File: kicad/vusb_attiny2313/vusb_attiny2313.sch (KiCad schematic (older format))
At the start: 24 parts, among them J1 USB_B_Micro, J2 PORT, J3 PORT B, J4 PORT A, Q1 BSS138, SW1 SW_SPST, U1 LM1117-1.8, U2 ATTINY2313-20PU, U3 MCP23S17, Y1 12Mhz

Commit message: first revision, kernel and avr part work. Kernel code have to be refine
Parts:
- removed SW1: SW_SPST, Buttons_Switches_THT:Nidec_Copal_SH-7010C, symbol Switch:SW_SPST
- added MK1, MK2: Mounting_Hole, Mounting_Holes:MountingHole_3.2mm_M3, symbol Mechanical:Mounting_Hole
- added SW2: SW_DIP_x03, Buttons_Switches_THT:SW_PUSH_x2, symbol Switch:SW_DIP_x03
- J1: footprint Connectors:USB_Mini-B -> Pin_Headers:Pin_Header_Straight_1x04_Pitch2.54mm
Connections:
- net labels added: DATA_CS, DATA_IN, DATA_OUT, DATA_SCK, LED
- wire segments 100 -> 99
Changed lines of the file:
@@
 F 0 "J1" H 1705 2017 50  0000 C CNN
 F 1 "USB_B_Micro" H 1705 1926 50  0000 C CNN
-F 2 "Connectors:USB_Mini-B" H 1800 1500 50  0001 C CNN
+F 2 "Pin_Headers:Pin_Header_Straight_1x04_Pitch2.54mm" H 1800 1500 50  0001 C CNN
 F 3 "~" H 1800 1500 50  0001 C CNN
 	1    1650 1550
@@
 	2850 1650 2600 1650
 Wire Wire Line
-	1950 1350 2200 1350
+	1950 1350 2100 1350
 $Comp
 L device:C_Small C6
@@
 	7500 2450 7500 2550
 $Comp
-L Switch:SW_SPST SW1
-U 1 1 5A423A7A
-P 2400 1350
-F 0 "SW1" H 2400 1585 50  0000 C CNN
-F 1 "SW_SPST" H 2400 1494 50  0000 C CNN
-F 2 "Buttons_Switches_THT:Nidec_Copal_SH-7010C" H 2400 1350 50  0001 C CNN
-F 3 "" H 2400 1350 50  0001 C CNN
-	1    2400 1350
-	1    0    0    -1
-$EndComp
-Wire Wire Line
-	2600 1350 3600 1350
-$Comp
 L Connector:Conn_01x10 J3
 U 1 1 5A423FF6
@@
 Wire Wire Line
 	9800 3500 9450 3500
-Wire Wire Line
-	6550 2700 6750 2700
-Wire Wire Line
-	6750 2250 6750 2700
 $Comp
 L Connector:Conn_01x04 J2
@@
 $EndComp
 Wire Wire Line
-	7500 3700 7500 2800
-Wire Wire Line
 	6750 2250 7200 2250
 Wire Wire Line
-	7500 2800 8450 2800
-Wire Wire Line
-	7600 2900 7600 4000
-Wire Wire Line
-	7600 2900 8450 2900
-Wire Wire Line
-	7700 4100 7700 3000
-Wire Wire Line
 	7700 3000 8450 3000
 Wire Wire Line
-	7800 3100 7800 4200
-Wire Wire Line
-	7800 3100 8450 3100
-Wire Wire Line
 	7050 3100 6550 3100
-Wire Wire Line
-	6550 4000 7600 4000
-Wire Wire Line
-	6550 4100 7700 4100
-Wire Wire Line
-	6550 4200 7800 4200
-Wire Wire Line
-	6550 3700 7500 3700
 Wire Wire Line
 	6550 3000 7050 3000
@@
 Wire Wire Line
 	10450 2800 10500 2800
+$Comp
+L Switch:SW_DIP_x03 SW2
+U 1 1 5A48211F
+P 2400 1350
+F 0 "SW2" H 2400 1817 50  0000 C CNN
+F 1 "SW_DIP_x03" H 2400 1726 50  0000 C CNN
+F 2 "Buttons_Switches_THT:SW_PUSH_x2" H 2400 1350 50  0001 C CNN
+F 3 "" H 2400 1350 50  0001 C CNN
+	1    2400 1350
+	1    0    0    -1
+$EndComp
+Connection ~ 2100 1350
+Connection ~ 2700 1350
+Wire Wire Line
+	2700 1350 3600 1350
+Wire Wire Line
+	2700 1350 2700 1250
+Wire Wire Line
+	2700 1250 2700 1150
+Connection ~ 2700 1250
+Wire Wire Line
+	2100 1150 2100 1250
+Wire Wire Line
+	2100 1250 2100 1350
+Connection ~ 2100 1250
+Text Label 6750 2250 0    50   ~ 0
+LED
+Text Label 7050 4100 2    50   ~ 0
+LED
+Wire Wire Line
+	7050 4100 6550 4100
+Wire Wire Line
+	6550 2700 7050 2700
+Text Label 7050 4200 2    50   ~ 0
+DATA_IN
+Text Label 7700 3000 0    50   ~ 0
+DATA_IN
+Text Label 7050 4000 2    50   ~ 0
+DATA_OUT
+Text Label 7700 3100 0    50   ~ 0
+DATA_OUT
+Wire Wire Line
+	7700 3100 8450 3100
+Wire Wire Line
+	7700 2900 8450 2900
+Wire Wire Line
+	7050 4200 6550 4200
+Text Label 7700 2900 0    50   ~ 0
+DATA_SCK
+Text Label 7050 2700 2    50   ~ 0
+DATA_SCK
+Text Label 7700 2800 0    50   ~ 0
+DATA_CS
+Wire Wire Line
+	7700 2800 8450 2800
+Text Label 7050 3700 2    50   ~ 0
+DATA_CS
+Wire Wire Line
+	6550 3700 7050 3700
+Wire Wire Line
+	6550 4000 7050 4000
+$Comp
+L Mechanical:Mounting_Hole MK2
+U 1 1 5A485C34
+P 1450 6350
+F 0 "MK2" H 1550 6396 50  0000 L CNN
+F 1 "Mounting_Hole" H 1550 6305 50  0000 L CNN
+F 2 "Mounting_Holes:MountingHole_3.2mm_M3" H 1450 6350 50  0001 C CNN
+F 3 "" H 1450 6350 50  0001 C CNN
+	1    1450 6350
+	1    0    0    -1
+$EndComp
+$Comp
+L Mechanical:Mounting_Hole MK1
+U 1 1 5A485DC0
+P 1450 6100
+F 0 "MK1" H 1550 6146 50  0000 L CNN
+F 1 "Mounting_Hole" H 1550 6055 50  0000 L CNN
+F 2 "Mounting_Holes:MountingHole_3.2mm_M3" H 1450 6100 50  0001 C CNN
+F 3 "" H 1450 6100 50  0001 C CNN
+	1    1450 6100
+	1    0    0    -1
+$EndComp
 $EndSCHEMATC

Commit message: add 27c256
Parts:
- removed J3: PORT B, Socket_Strips:Socket_Strip_Straight_1x10_Pitch2.54mm, symbol Connector:Conn_01x10
- removed U3: MCP23S17, Housings_DIP:DIP-28_W7.62mm_LongPads, symbol microchip:MCP23S17
- added U?: 27C256, Package_DIP:DIP-28_W15.24mm, symbol Memory_EPROM:27C256
- C1, C3, C4, C6: symbol device:C_Small -> vusb_attiny2313-rescue:C_Small-device
- C2, C5: symbol device:CP1_Small -> vusb_attiny2313-rescue:CP1_Small-device
- D1: symbol device:LED_Small -> vusb_attiny2313-rescue:LED_Small-device
- ISP1: symbol atmel:AVR-ISP-6 -> vusb_attiny2313-rescue:AVR-ISP-6-atmel
- J2: symbol Connector:Conn_01x04 -> vusb_attiny2313-rescue:Conn_01x04-Connector
- J4: symbol Connector:Conn_01x08 -> vusb_attiny2313-rescue:Conn_01x08-Connector
- MK1, MK2: symbol Mechanical:Mounting_Hole -> vusb_attiny2313-rescue:Mounting_Hole-Mechanical
- Q1: symbol Transistor:BSS138 -> vusb_attiny2313-rescue:BSS138-Transistor
- R1, R2, R3, R4, R5, R6: symbol device:R_Small -> vusb_attiny2313-rescue:R_Small-device
- U1: value LM1117-1.8 -> LM1117-3.3; symbol regul:LM1117-1.8 -> vusb_attiny2313-rescue:LM1117-1.8-regul
- U2: symbol atmel:ATTINY2313-20PU -> vusb_attiny2313-rescue:ATTINY2313-20PU-atmel
- Y1: symbol device:Crystal_Small -> vusb_attiny2313-rescue:Crystal_Small-device
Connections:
- net labels added: D0, D1, D2, D3, D4, D5, D6, D7, D[0..7]
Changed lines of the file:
@@
 $EndDescr
 $Comp
-L atmel:ATTINY2313-20PU U2
+L vusb_attiny2313-rescue:ATTINY2313-20PU-atmel U2
 U 1 1 5A3E5479
 P 5400 3500
@@
 $EndComp
 $Comp
-L regul:LM1117-1.8 U1
+L vusb_attiny2313-rescue:LM1117-1.8-regul U1
 U 1 1 5A3E55A4
 P 4050 1350
 F 0 "U1" H 4050 1592 50  0000 C CNN
-F 1 "LM1117-1.8" H 4050 1501 50  0000 C CNN
+F 1 "LM1117-3.3" H 4050 1501 50  0000 C CNN
 F 2 "TO_SOT_Packages_SMD:SOT-223-3_TabPin2" H 4050 1350 50  0001 C CNN
 F 3 "http://www.ti.com/lit/ds/symlink/lm1117.pdf" H 4050 1350 50  0001 C CNN
@@
 $EndComp
 $Comp
-L device:Crystal_Small Y1
+L vusb_attiny2313-rescue:Crystal_Small-device Y1
 U 1 1 5A3E5771
 P 4000 3100
@@
 $EndComp
 $Comp
-L device:C_Small C3
+L vusb_attiny2313-rescue:C_Small-device C3
 U 1 1 5A3E586E
 P 3650 3500
@@
 $EndComp
 $Comp
-L device:C_Small C4
+L vusb_attiny2313-rescue:C_Small-device C4
 U 1 1 5A3E590E
 P 4000 3500
@@
 $EndComp
 $Comp
-L atmel:AVR-ISP-6 ISP1
+L vusb_attiny2313-rescue:AVR-ISP-6-atmel ISP1
 U 1 1 5A3E59A3
 P 1550 4600
@@
 $EndComp
 $Comp
-L device:R_Small R4
+L vusb_attiny2313-rescue:R_Small-device R4
 U 1 1 5A3E5B40
 P 3100 1150
@@
 $EndComp
 $Comp
-L device:R_Small R3
+L vusb_attiny2313-rescue:R_Small-device R3
 U 1 1 5A3E5BC7
 P 2850 1150
@@
 $EndComp
 $Comp
-L device:R_Small R1
+L vusb_attiny2313-rescue:R_Small-device R1
 U 1 1 5A3E5C29
 P 2200 1550
@@
 $EndComp
 $Comp
-L device:R_Small R2
+L vusb_attiny2313-rescue:R_Small-device R2
 U 1 1 5A3E5CDB
 P 2500 1650
@@
 $EndComp
 $Comp
-L device:CP1_Small C2
+L vusb_attiny2313-rescue:CP1_Small-device C2
 U 1 1 5A3E5D76
 P 3600 1600
@@
 $EndComp
 $Comp
-L device:CP1_Small C5
+L vusb_attiny2313-rescue:CP1_Small-device C5
 U 1 1 5A3E5F04
 P 4600 1600
@@
 $EndComp
 $Comp
-L device:R_Small R5
+L vusb_attiny2313-rescue:R_Small-device R5
 U 1 1 5A3E5F38
 P 3350 2500
@@
 	1950 1350 2100 1350
 $Comp
-L device:C_Small C6
+L vusb_attiny2313-rescue:C_Small-device C6
 U 1 1 5A3E725E
 P 5000 1600
@@
 	3350 2700 4250 2700
 $Comp
-L device:C_Small C1
+L vusb_attiny2313-rescue:C_Small-device C1
 U 1 1 5A3E918A
 P 3350 2900
@@
 Text Label 6850 3900 2    50   ~ 0
 D-
-$Comp
-L microchip:MCP23S17 U3
-U 1 1 5A3F3039
-P 8950 2700
-F 0 "U3" H 8950 2850 50  0000 C CNN
-F 1 "MCP23S17" H 8950 2700 50  0000 C CNN
-F 2 "Housings_DIP:DIP-28_W7.62mm_LongPads" H 9000 1750 50  0001 L CNN
-F 3 "http://ww1.microchip.com/downloads/en/DeviceDoc/20001952C.pdf" H 9200 3700 50  0001 C CNN
-	1    8950 2700
-	-1   0    0    -1
-$EndComp
 Wire Wire Line
 	8450 2400 8000 2400
@@
 $EndComp
 $Comp
-L device:R_Small R6
+L vusb_attiny2313-rescue:R_Small-device R6
 U 1 1 5A400338
 P 7500 1400
@@
 	7500 1200 7500 1300
 $Comp
-L device:LED_Small D1
+L vusb_attiny2313-rescue:LED_Small-device D1
 U 1 1 5A40196B
 P 7500 1700
@@
 $EndComp
 $Comp
-L Transistor:BSS138 Q1
+L vusb_attiny2313-rescue:BSS138-Transistor Q1
 U 1 1 5A406ED6
 P 7400 2250
@@
 	7500 2450 7500 2550
 $Comp
-L Connector:Conn_01x10 J3
-U 1 1 5A423FF6
-P 10700 2300
-F 0 "J3" H 10780 2292 50  0000 L CNN
-F 1 "PORT B" H 10780 2201 50  0000 L CNN
-F 2 "Socket_Strips:Socket_Strip_Straight_1x10_Pitch2.54mm" H 10700 2300 50  0001 C CNN
-F 3 "~" H 10700 2300 50  0001 C CNN
-	1    10700 2300
-	1    0    0    -1
-$EndComp
-$Comp
-L Connector:Conn_01x08 J4
+L vusb_attiny2313-rescue:Conn_01x08-Connector J4
 U 1 1 5A4240DB
 P 10000 3100
@@
 	9800 3500 9450 3500
 $Comp
-L Connector:Conn_01x04 J2
+L vusb_attiny2313-rescue:Conn_01x04-Connector J2
 U 1 1 5A4059D7
 P 7250 2900
@@
 $EndComp
 Wire Wire Line
-	9450 1900 10500 1900
-Wire Wire Line
-	9450 2000 10500 2000
-Wire Wire Line
-	9450 2100 10500 2100
-Wire Wire Line
-	9450 2200 10500 2200
-Wire Wire Line
-	9450 2300 10500 2300
-Wire Wire Line
-	9450 2400 10500 2400
-Wire Wire Line
-	9450 2500 10500 2500
-Wire Wire Line
-	9450 2600 10500 2600
-Wire Wire Line
 	10300 2900 10300 2700
 Wire Wire Line
@@
 	6550 4000 7050 4000
 $Comp
-L Mechanical:Mounting_Hole MK2
+L vusb_attiny2313-rescue:Mounting_Hole-Mechanical MK2
 U 1 1 5A485C34
 P 1450 6350
@@
 $EndComp
 $Comp
-L Mechanical:Mounting_Hole MK1
+L vusb_attiny2313-rescue:Mounting_Hole-Mechanical MK1
 U 1 1 5A485DC0
 P 1450 6100
@@
 	1    0    0    -1
 $EndComp
+$Comp
+L Memory_EPROM:27C256 U?
+U 1 1 5D263362
+P 8950 2600
+F 0 "U?" H 8950 3878 50  0000 C CNN
+F 1 "27C256" H 8950 3787 50  0000 C CNN
+F 2 "Package_DIP:DIP-28_W15.24mm" H 8950 2600 50  0001 C CNN
+F 3 "http://ww1.microchip.com/downloads/en/DeviceDoc/doc0014.pdf" H 8950 2600 50  0001 C CNN
+	1    8950 2600
+	1    0    0    -1
+$EndComp
+Entry Wire Line
+	9550 1700 9650 1800
+Entry Wire Line
+	9550 1800 9650 1900
+Entry Wire Line
+	9550 1900 9650 2000
+Entry Wire Line
+	9550 2000 9650 2100
+Entry Wire Line
+	9550 2100 9650 2200
+Entry Wire Line
+	9550 2200 9650 2300
+Entry Wire Line
+	9550 2300 9650 2400
+Entry Wire Line
+	9550 2400 9650 2500
+Wire Wire Line
+	9350 1700 9550 1700
+Wire Bus Line
+	9650 1500 9650 2650
+Wire Wire Line
+	9350 1800 9550 1800
+Wire Wire Line
+	9350 1900 9550 1900
+Wire Wire Line
+	9350 2000 9550 2000
+Wire Wire Line
+	9350 2100 9550 2100
+Wire Wire Line
+	9350 2200 9550 2200
+Wire Wire Line
+	9350 2300 9550 2300
+Wire Wire Line
+	9350 2400 9550 2400
+Text Label 9400 1700 0    50   ~ 0
+D0
+Text Label 9400 1800 0    50   ~ 0
+D1
+Text Label 9400 1900 0    50   ~ 0
+D2
+Text Label 9400 2000 0    50   ~ 0
+D3
+Text Label 9400 2100 0    50   ~ 0
+D4
+Text Label 9400 2200 0    50   ~ 0
+D5
+Text Label 9400 2300 0    50   ~ 0
+D6
+Text Label 9400 2400 0    50   ~ 0
+D7
+Text Label 9650 1500 3    50   ~ 0
+D[0..7]
 $EndSCHEMATC

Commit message: schematic done
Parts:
- removed C5: 10µ, Capacitors_THT:CP_Radial_D5.0mm_P2.50mm, symbol vusb_attiny2313-rescue:CP1_Small-device
- removed C6: 100n, Capacitors_SMD:C_0805_HandSoldering, symbol vusb_attiny2313-rescue:C_Small-device
- removed J1: USB_B_Micro, Pin_Headers:Pin_Header_Straight_1x04_Pitch2.54mm, symbol Connector:USB_B_Micro
- removed J2: PORT, Socket_Strips:Socket_Strip_Straight_1x04_Pitch2.54mm, symbol vusb_attiny2313-rescue:Conn_01x04-Connector
- removed J4: PORT A, Socket_Strips:Socket_Strip_Straight_1x08_Pitch2.54mm, symbol vusb_attiny2313-rescue:Conn_01x08-Connector
- removed U1: LM1117-3.3, TO_SOT_Packages_SMD:SOT-223-3_TabPin2, symbol vusb_attiny2313-rescue:LM1117-1.8-regul
- added D2, D5: SD 103BW, Diode_SMD:D_SOD-123, symbol Device:D_Schottky_Small
- added D3, D4: 1N4148, Diode_SMD:D_MiniMELF_Handsoldering, symbol Device:D_Small
- added J1: USB, Connector_PinHeader_2.54mm:PinHeader_1x04_P2.54mm_Vertical, symbol Connector_Generic:Conn_01x04
- added Q2: BSS138, Package_TO_SOT_SMD:SOT-23, symbol vusb_attiny2313-rescue:BSS138-Transistor
- added U1, U3, U4: 74HC595, Package_DIP:DIP-16_W7.62mm_Socket_LongPads, symbol 74xx:74HC595
- C1, C3, C4: footprint Capacitors_SMD:C_0805_HandSoldering -> Capacitor_SMD:C_0805_2012Metric_Pad1.15x1.40mm_HandSolder
- C2: footprint Capacitors_THT:CP_Radial_D5.0mm_P2.50mm -> Capacitor_THT:CP_Radial_D5.0mm_P2.50mm
- D1: footprint LEDs:LED_D3.0mm -> LED_THT:LED_D3.0mm
- ISP1: footprint Pin_Headers:Pin_Header_Straight_2x03_Pitch2.54mm -> Connector_PinHeader_2.54mm:PinHeader_2x03_P2.54mm_Vertical
- MK1, MK2: footprint Mounting_Holes:MountingHole_3.2mm_M3 -> MountingHole:MountingHole_3.2mm_M3
- Q1: footprint TO_SOT_Packages_SMD:SOT-23 -> Package_TO_SOT_SMD:SOT-23
- R1, R2, R3, R4, R5: footprint Resistors_SMD:R_1206 -> Resistor_SMD:R_0805_2012Metric_Pad1.15x1.40mm_HandSolder
- R6: value 470 -> 960; footprint Resistors_SMD:R_1206 -> Resistor_SMD:R_0805_2012Metric_Pad1.15x1.40mm_HandSolder
- SW2: footprint Buttons_Switches_THT:SW_PUSH_x2 -> modules:DPDT_WIDE_54_54
- U2: footprint Housings_DIP:DIP-20_W7.62mm -> Package_DIP:DIP-20_W7.62mm_LongPads
- U5: renamed from U?; footprint Package_DIP:DIP-28_W15.24mm -> modules:DIP_Socket-28pin_in_32_W11.9_W12.7_W15.24_W17.78_W18.5_3M_232-1285-00-0602J
- Y1: footprint Crystals:Crystal_SMD_HC49-SD -> Crystal:Crystal_HC49-U_Vertical
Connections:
- net labels added: +12V, +5V, A10, A11, A12, A13, A14, A8, A9, A9_, A9_set, DATA_CLR, DATA_Q, DATA_R, VPP, VPP_set, ~CE, ~OE, ~VPP
- net labels removed: DATA_OUT, INTA, INTB, LED
- wire segments 99 -> 138
- no-connect marks 2 -> 7
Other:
- moved on the sheet: C1, C3, C4, D1, ISP1, MK1, MK2, Q1, R5, R6, U2, U5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

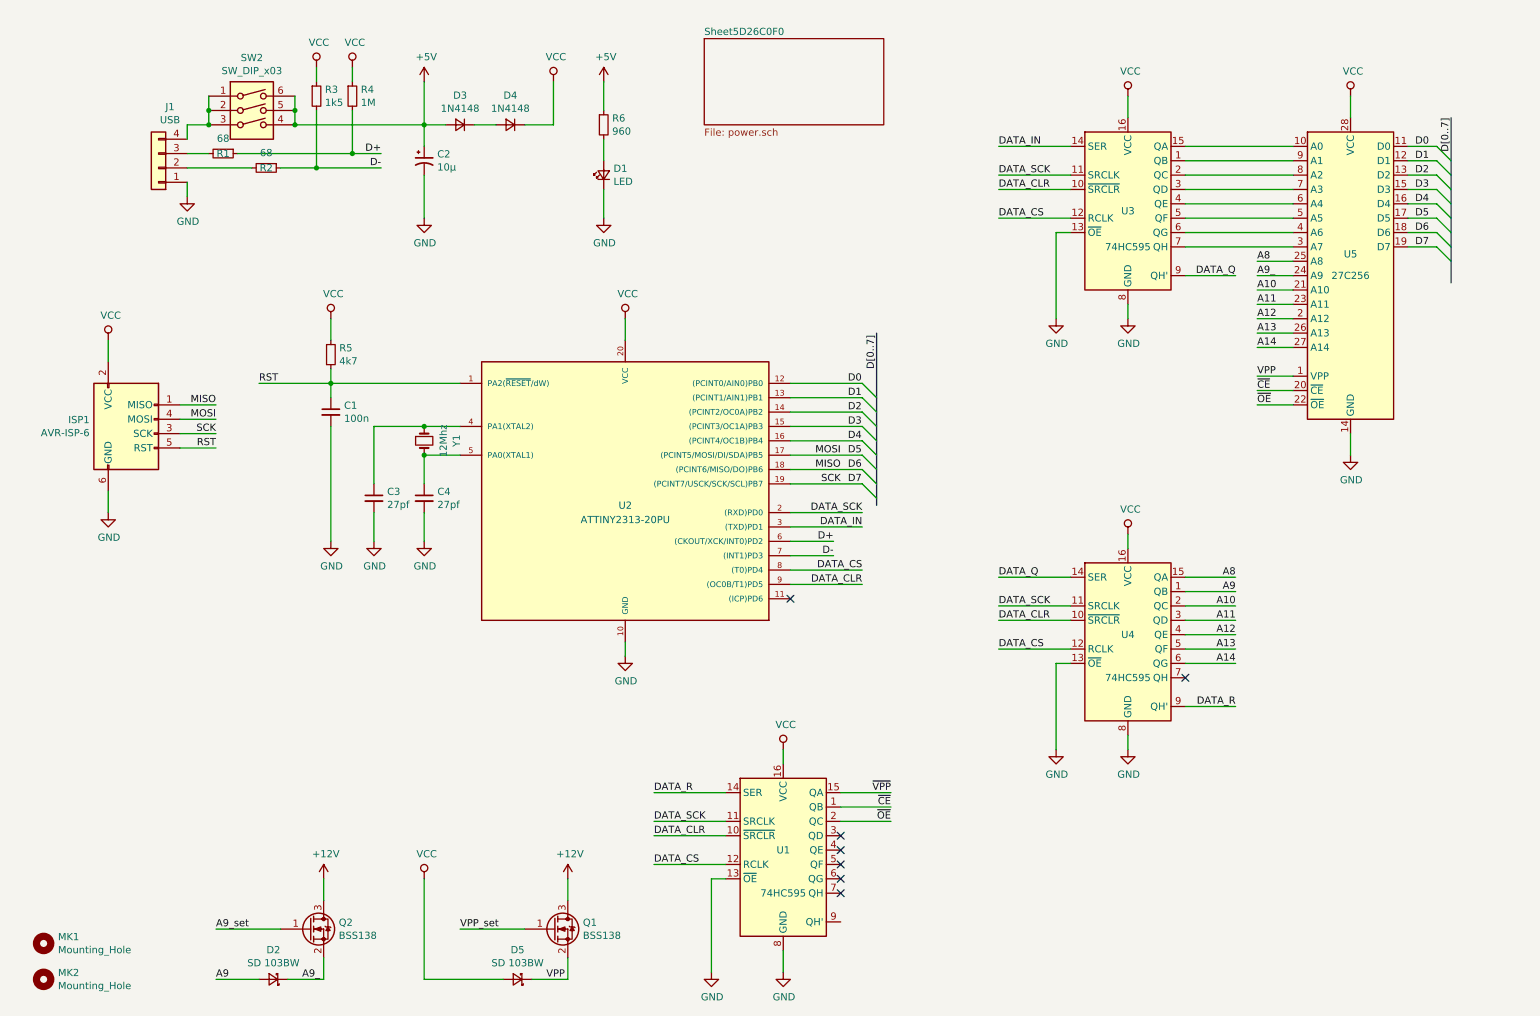
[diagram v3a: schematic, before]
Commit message: fuses angepasst!
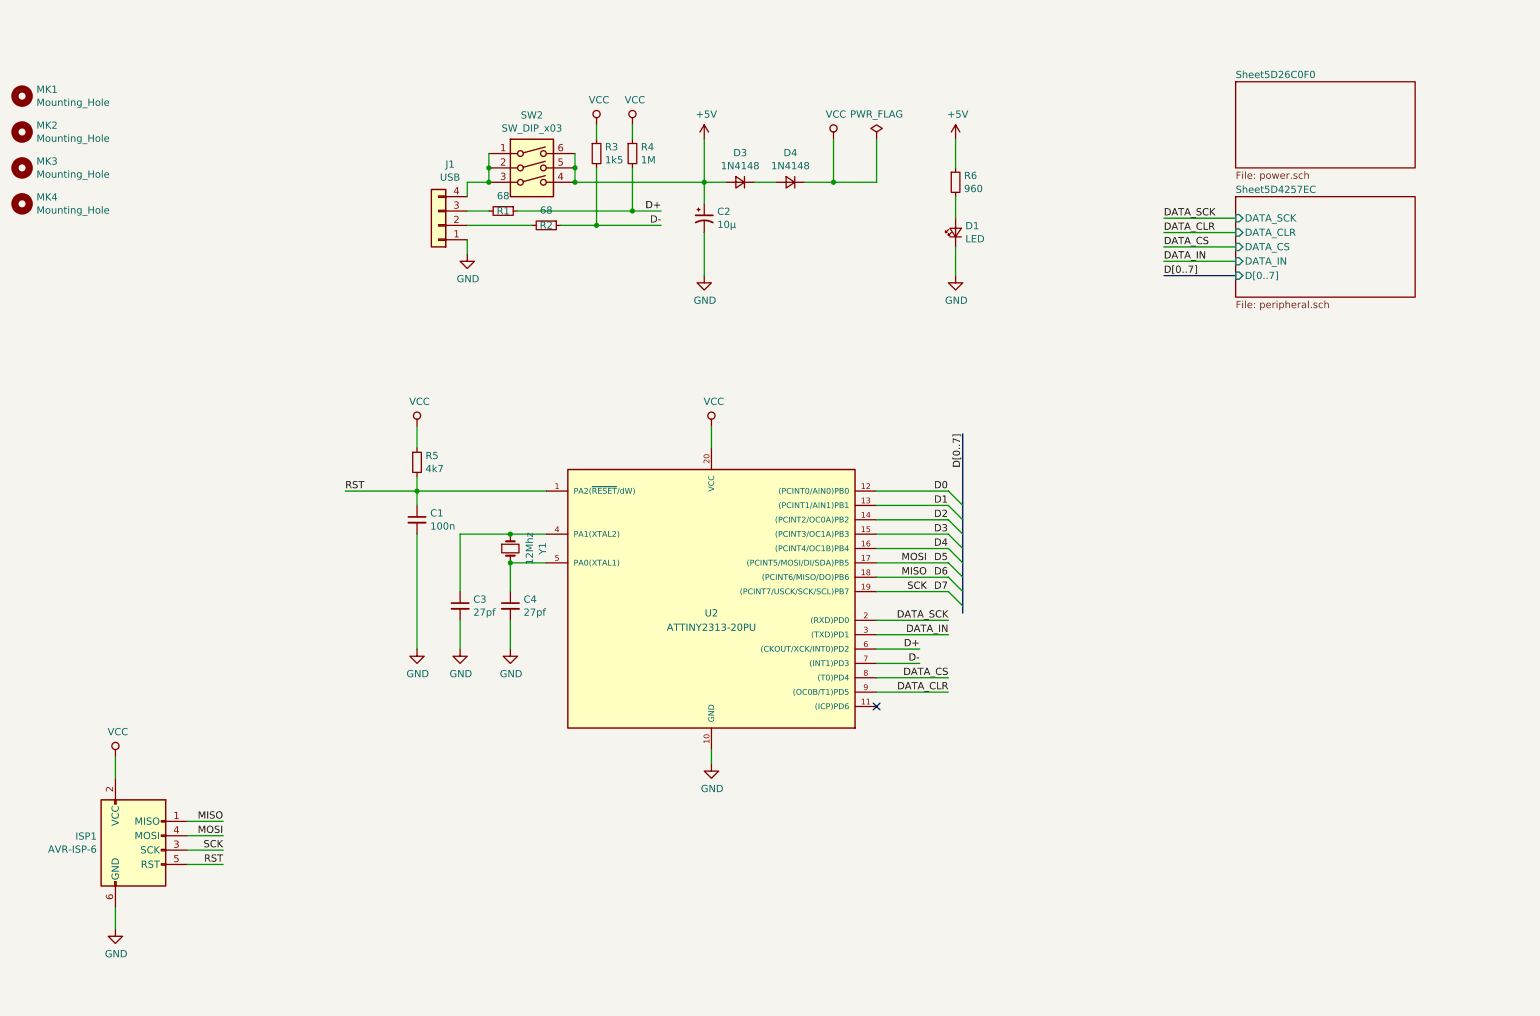
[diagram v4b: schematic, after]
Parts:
- removed D2, D5: SD 103BW, Diode_SMD:D_SOD-123, symbol Device:D_Schottky_Small
- removed Q1, Q2: BSS138, Package_TO_SOT_SMD:SOT-23, symbol vusb_attiny2313-rescue:BSS138-Transistor
- removed U1, U3, U4: 74HC595, Package_DIP:DIP-16_W7.62mm_Socket_LongPads, symbol 74xx:74HC595
- removed U5: 27C256, modules:DIP_Socket-28pin_in_32_W11.9_W12.7_W15.24_W17.78_W18.5_3M_232-1285-00-0602J, symbol Memory_EPROM:27C256
- added MK3, MK4: Mounting_Hole, MountingHole:MountingHole_3.2mm_M3, symbol vusb_attiny2313-rescue:Mounting_Hole-Mechanical
- D1: footprint LED_THT:LED_D3.0mm -> LED_SMD:LED_1206_3216Metric_Pad1.42x1.75mm_HandSolder
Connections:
- no-connect marks 7 -> 1
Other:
- moved on the sheet: C1, C2, C3, C4, D1, D3, D4, ISP1, J1, MK1, MK2, R1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
